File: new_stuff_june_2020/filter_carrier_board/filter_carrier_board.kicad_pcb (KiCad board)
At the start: 2 copper layers, 99.1 x 99.1 mm, 44 parts, among them J1 CV_inputs, J10 Conn_02x05_Odd_Even, J2 signal_inputs, J3 dry_out, J4 Conn_01x04, J5 Conn_01x04, J6 CV_out, J7 Conn_01x04, J8 Conn_01x08, J9 wet_out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

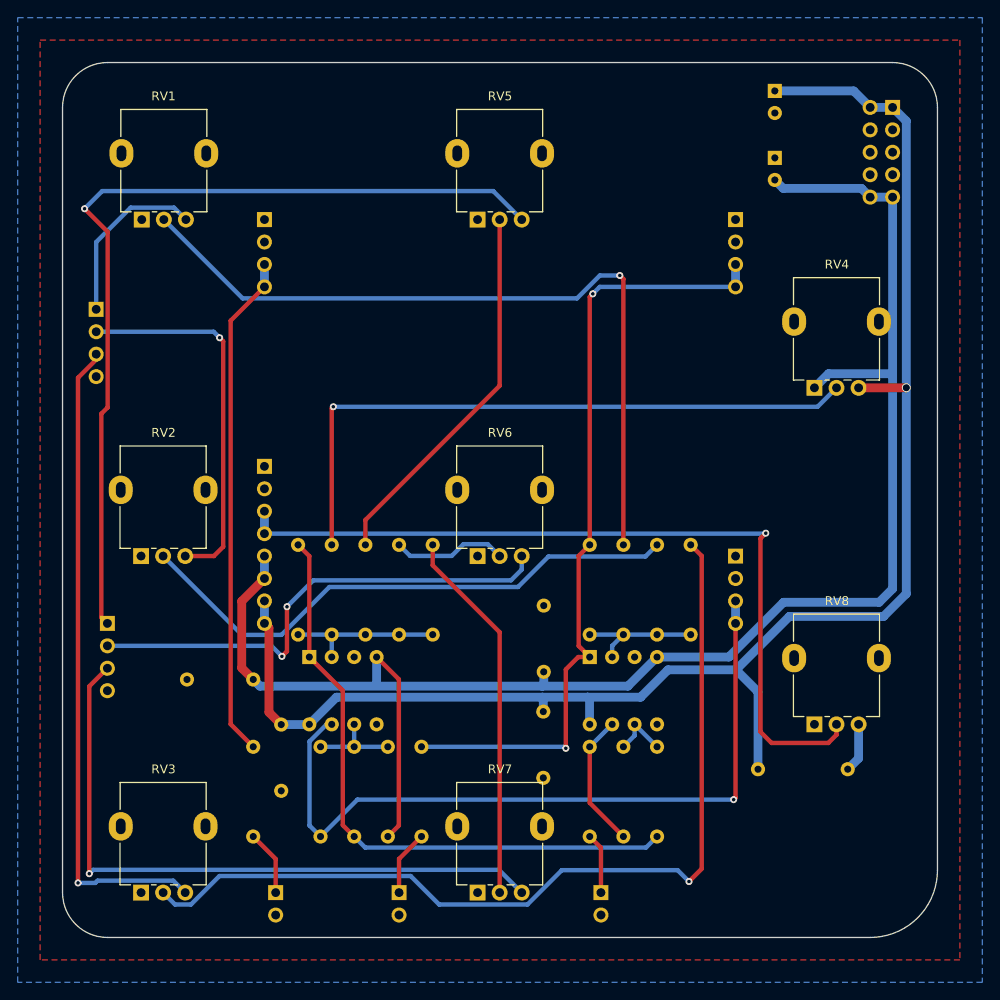
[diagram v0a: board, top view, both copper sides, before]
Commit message: add +/- 5 volt ref to VCF carrier board
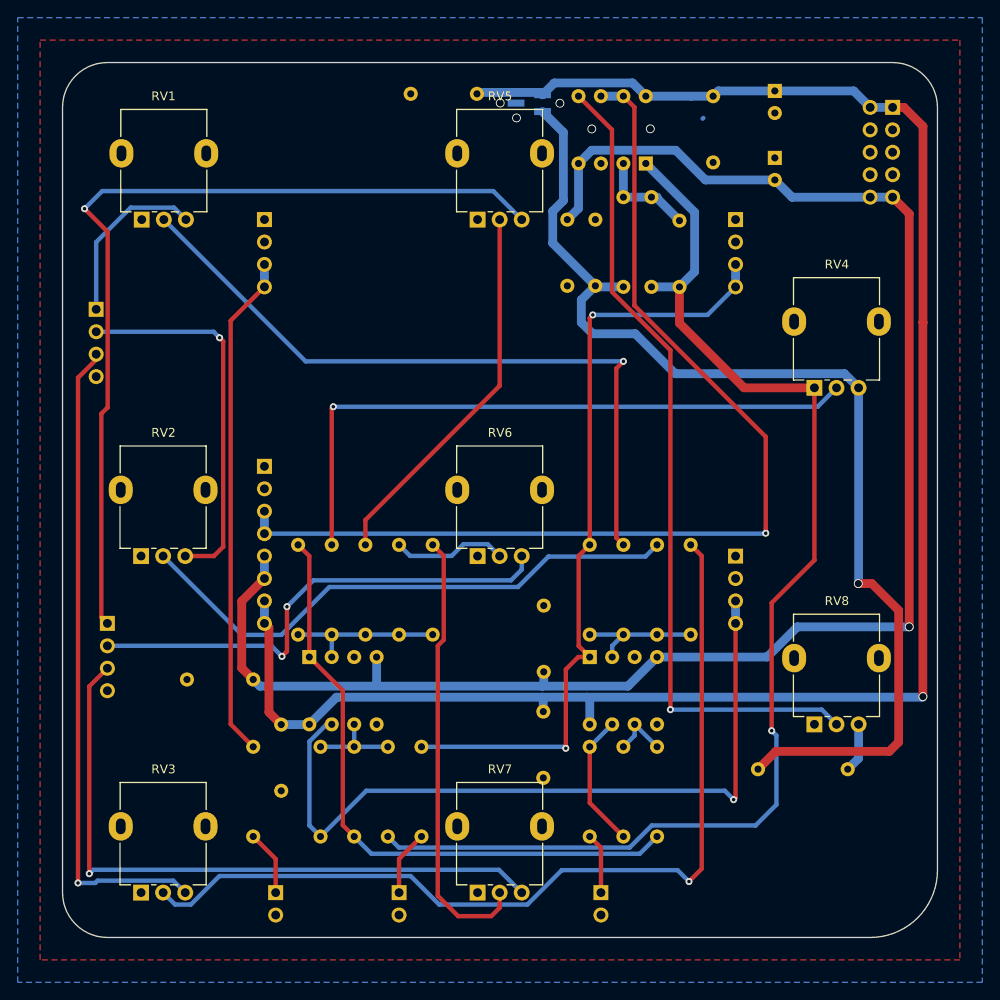
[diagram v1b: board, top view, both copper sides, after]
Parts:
- added C10: 100nF, Capacitor_THT:C_Axial_L3.8mm_D2.6mm_P7.50mm_Horizontal, B.Cu at (175.3, 54.6)
- added C11: 100nF, Capacitor_THT:C_Axial_L3.8mm_D2.6mm_P7.50mm_Horizontal, B.Cu at (158.8, 76.1)
- added C7: 100nF, Capacitor_THT:C_Axial_L3.8mm_D2.6mm_P7.50mm_Horizontal, B.Cu at (148.5, 54.3)
- added C8: 100nF, Capacitor_THT:C_Axial_L3.8mm_D2.6mm_P7.50mm_Horizontal, B.Cu at (161.9, 76.1)
- added C9: 100nF, Capacitor_THT:C_Axial_L3.8mm_D2.6mm_P7.50mm_Horizontal, B.Cu at (171.4, 68.7)
- added R19: 10k, Resistor_THT:R_Axial_DIN0207_L6.3mm_D2.5mm_P10.16mm_Horizontal, B.Cu at (165.1, 66.0)
- added R20: 10k, Resistor_THT:R_Axial_DIN0207_L6.3mm_D2.5mm_P10.16mm_Horizontal, B.Cu at (168.3, 76.2)
- added U3: MAX6035xxUR50, Package_TO_SOT_SMD:SOT-23_Handsoldering, B.Cu at (154.4, 55.4)
- added U4: TL072, Package_DIP:DIP-8_W7.62mm, B.Cu at (167.6, 62.2)
- R10: value 240k -> ???
- R15: value 22k -> 100k
- R18: value 47k -> 12k
- R4: value 240k -> 100k
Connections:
- R10 pad 2: -12V -> -5V
- R18 pad 1: +12V -> +5V
- RV4 pad 1: -12V -> -5V
- RV4 pad 3: +12V -> +5V
- RV8 pad 2: Net-(J8-Pad3) -> Net-(RV8-Pad2)
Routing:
- net -5V: track 0.00 -> 138.5 mm, vias 0 -> 1
- net +5V: track 0.00 -> 125.8 mm, vias 0 -> 1
- net Net-(RV8-Pad2): track 0.00 -> 93.3 mm, vias 0 -> 1
- net +12V: track 184.4 -> 212.0 mm
- net Net-(J8-Pad3): track 92.8 -> 118.0 mm
- net Net-(C9-Pad1): track 0.00 -> 12.5 mm
- net Net-(R7-Pad2): track 42.5 -> 50.6 mm
- net Net-(R1-Pad2): track 87.1 -> 80.1 mm
- net -12V: track 187.8 -> 192.6 mm, vias 0 -> 1
- net Net-(J4-Pad3): track 90.0 -> 88.6 mm
- net Net-(J5-Pad3): track 85.7 -> 86.5 mm
- net Net-(R11-Pad2): track 71.0 -> 71.6 mm
- net GND: track 0.00 -> 0.12 mm, vias 0 -> 5
